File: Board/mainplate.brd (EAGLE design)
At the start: 36.5 x 36.8 mm, 29 parts, among them U1 M24C04-WMN6P, U2 PCF8563T/F4,118, U3 STM32F103CBT6, X1 22-23-2091, X2 22-23-2041

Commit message: Process commit
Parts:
- added AUDIO_1, AUDIO_2, BTN_IN, BTN_OUT, USB_DM, USB_DP, USB_GND, USB_VCC: (no value), wirepad:2,54/1,0
- moved LED_G 3.81 mm to (14.0, 77.5)
- moved LED_R 3.81 mm to (10.2, 77.5)
- moved LED_GND 3.81 mm to (6.35, 77.5)
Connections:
- net N$16 renamed LED_G
- net N$17 renamed LED_R
- removed net N$15: LED_GND.1
- removed net NFC_RESET: U3.13
- new net AUDIO_1: AUDIO_1.1
- new net USB_DM: USB_DM.1
- new net USB_DP: USB_DP.1
- new net USB_VCC: USB_VCC.1
- net GND: now also AUDIO_2.1, LED_GND.1, USB_GND.1
- net NFC_RST: now also U3.13
- net VBAT: now also BTN_IN.1
- net VBAT2: now also BTN_OUT.1
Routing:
- net 3_3V: track 0.00 -> 56.5 mm, vias 0 -> 4
- net GND: track 0.00 -> 20.7 mm, vias 0 -> 9
- net N$9: track 0.00 -> 9.77 mm
- net N$6: track 0.00 -> 8.35 mm
- net N$7: track 0.00 -> 7.45 mm
- net N$4: track 0.00 -> 6.03 mm
- net EE_WC: track 0.00 -> 4.00 mm
- net N$11: track 0.00 -> 2.91 mm
- net N$10: track 0.00 -> 2.88 mm

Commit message: plate process
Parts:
- Q2: device crystal-geyer_V1_0:3.2X2.5_KX-7 -> crystal-geyer_V1_0:11.4X4.5
- moved USB_GND 8.13 mm to (2.54, 45.7)
- moved Q2 1.40 mm to (8.51, 62.0), turned to 90 degrees
- moved C3 0.38 mm to (29.1, 71.3)
- moved C2 0.18 mm to (33.1, 67.8)
- moved C1 0.13 mm to (29.2, 62.7)
- moved R1 0.13 mm to (29.2, 64.7)
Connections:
- net N$1: now also Q2.2; no longer Q2.3
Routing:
- net NFC_SS: track 0.00 -> 32.0 mm
- net 3_3V: track 56.5 -> 88.0 mm, vias 4 -> 7
- net NFC_SCK: track 0.00 -> 30.9 mm
- net NRST: track 0.00 -> 28.4 mm, vias 0 -> 2
- net NFC_MOSI: track 0.00 -> 24.8 mm, vias 0 -> 1
- net NFC_IOR: track 0.00 -> 23.5 mm, vias 0 -> 1
- net NFC_MISO: track 0.00 -> 21.9 mm, vias 0 -> 1
- net N$14: track 0.00 -> 17.4 mm, vias 0 -> 1
- net NFC_RST: track 0.00 -> 14.8 mm, vias 0 -> 1
- net N$13: track 0.00 -> 11.9 mm, vias 0 -> 1
- net N$8: track 0.00 -> 8.62 mm
- net N$1: track 3.41 -> 9.61 mm
- net GND: track 20.7 -> 26.4 mm
- net VBAT2: track 0.00 -> 4.40 mm
- net N$3: track 0.00 -> 3.91 mm
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- added copper zone on layer 1, net GND

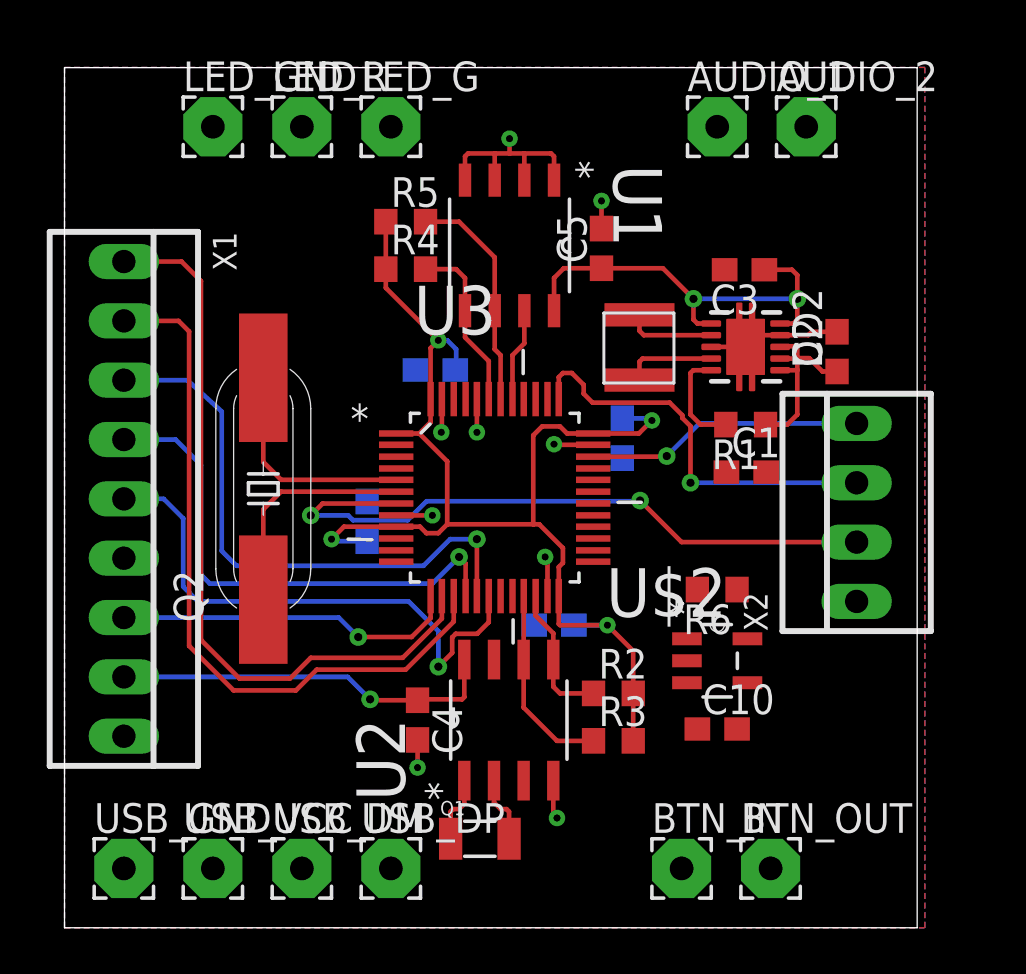
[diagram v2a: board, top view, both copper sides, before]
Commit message: First release version
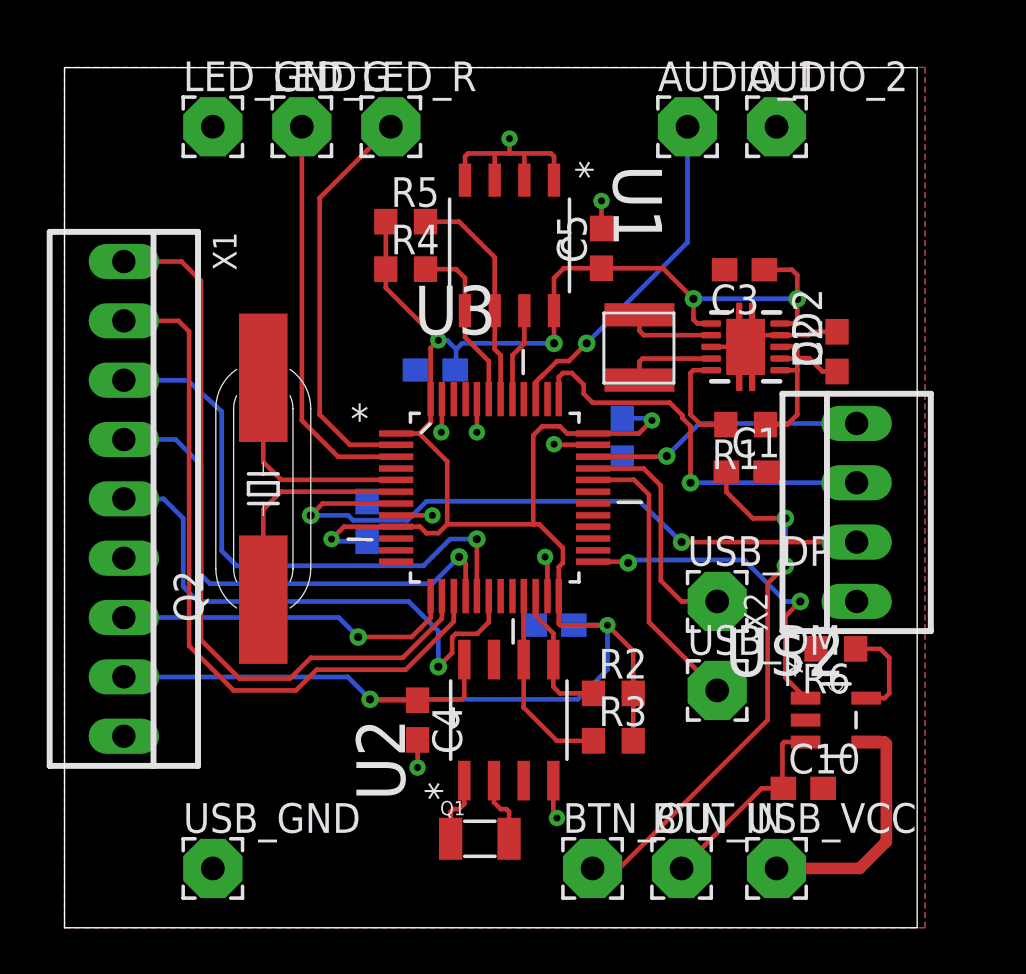
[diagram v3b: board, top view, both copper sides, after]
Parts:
- moved USB_VCC 24.1 mm to (30.5, 45.7)
- moved USB_DM 19.3 mm to (27.9, 53.3)
- moved USB_DP 18.1 mm to (27.9, 57.1)
- moved BTN_OUT 7.62 mm to (22.6, 45.7)
- moved R6 5.68 mm to (33.0, 55.1)
- moved U$2 5.68 mm to (33.0, 52.1)
- moved C10 4.47 mm to (31.6, 49.1)
- moved LED_G 3.81 mm to (10.2, 77.5)
- moved LED_R 3.81 mm to (14.0, 77.5)
- moved USB_GND 3.81 mm to (6.35, 45.7)
- moved AUDIO_1 1.27 mm to (26.7, 77.5)
- moved AUDIO_2 1.27 mm to (30.5, 77.5)
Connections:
- removed net PA11: U3.32
- removed net USB: U$2.4
- new net N$15: U$2.1, U3.25
- net AUDIO_1: now also U3.39
- net LED_G: now also U3.3
- net LED_R: now also U3.2
- net USB_DM: now also U3.32
- net USB_DP: now also U3.33
- net USB_VCC: now also U$2.4
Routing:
- net VBAT2: track 4.40 -> 27.3 mm, vias 0 -> 2
- net 3_3V: track 88.0 -> 106.3 mm, vias 7 -> 8
- net LED_R: track 0.00 -> 17.4 mm
- net LED_G: track 0.00 -> 17.3 mm
- net AUDIO_1: track 0.00 -> 14.7 mm, vias 0 -> 1
- net N$15: track 0.00 -> 14.4 mm, vias 0 -> 2
- net USB_DM: track 0.00 -> 12.2 mm
- net USB_VCC: track 0.00 -> 10.3 mm
- net USB_DP: track 0.00 -> 10.0 mm
- net VBAT: track 0.00 -> 8.85 mm
- net N$12: track 0.00 -> 4.19 mm
